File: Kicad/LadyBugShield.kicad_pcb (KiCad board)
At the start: 2 copper layers, 81.3 x 53.3 mm, 48 parts, among them P1 CONN_6, P2 CONN_2, P3 BNC, P4 BNC, Q1 TIP122, Q2 TIP122, Q3 TIP122, U1 MCP6244, U2 MCP6242, U3 MC78L05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

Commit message: 2nd iteration on layout
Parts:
- R2: value 1.5K 1% -> 1K 1%
- moved C1 33.1 mm to (222.9, 106.4), turned to 0 degrees
- moved D8 28.8 mm to (210.4, 80.3), turned to 90 degrees
- moved R1 24.7 mm to (184.3, 70.6)
- moved D7 23.2 mm to (194.1, 99.1), turned to 180 degrees
- moved C8 21.3 mm to (219.8, 97.3), turned to 0 degrees
- moved C6 20.9 mm to (202.8, 79.4), turned to 90 degrees
- moved R16 20.8 mm to (215.5, 89.2), turned to 0 degrees
- moved D6 19.2 mm to (193.8, 92.6), turned to 0 degrees
- moved D4 18.1 mm to (206.0, 80.4), turned to 270 degrees
- moved R4 17.7 mm to (209.4, 87.4), turned to 180 degrees
- moved R14 17.5 mm to (215.5, 91.4), turned to 180 degrees
- moved R13 17.4 mm to (208.4, 85.1), turned to 0 degrees
- moved C5 17.2 mm to (211.4, 89.6), turned to 0 degrees
- moved C7 16.0 mm to (215.5, 93.7), turned to 0 degrees
- moved R19 16.0 mm to (215.5, 96.0), turned to 0 degrees
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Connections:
- ARD1 pad 8: /Arduino/ALERT -> (no net)
- U4 pad 2: /Arduino/ALERT -> (no net)
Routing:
- net VClean: track 201.1 -> 264.5 mm, vias 3 -> 4
- net /EC/f1: track 56.5 -> 9.40 mm
- net /DigitalAccess/pH_AIN: track 50.9 -> 71.6 mm, vias 2 -> 0
- net /EC/EC_ProbeIN: track 24.3 -> 44.5 mm, vias 0 -> 2
- net /Arduino/Pump1: track 36.4 -> 20.4 mm
- net N-0000051: track 4.68 -> 18.8 mm
- net /Arduino/ALERT: track 13.8 -> 0.00 mm
- net /DigitalAccess/EC_AIN: track 26.2 -> 15.5 mm, vias 2 -> 0
- net /Pumps/SW_Pump1: track 17.5 -> 24.9 mm
- net VGND: track 136.6 -> 143.4 mm, vias 4 -> 1
- net AC_Shrunk: track 8.64 -> 14.5 mm
- net EC_Signal: track 20.8 -> 14.9 mm
- net /EC/RVin-: track 14.1 -> 19.9 mm
- net N-0000052: track 4.15 -> 8.63 mm
- net /Pumps/SW_Pump2: track 19.3 -> 23.7 mm
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
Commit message: update to 2nd pass of layout
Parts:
- moved R7 1.65 mm to (220.0, 108.9)
- moved R6 1.35 mm to (216.5, 109.0)
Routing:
- net GND: track 53.5 -> 50.0 mm, vias 16 -> 15
- net VClean: track 264.5 -> 262.4 mm
- net /Arduino/SDA: track 9.95 -> 10.8 mm

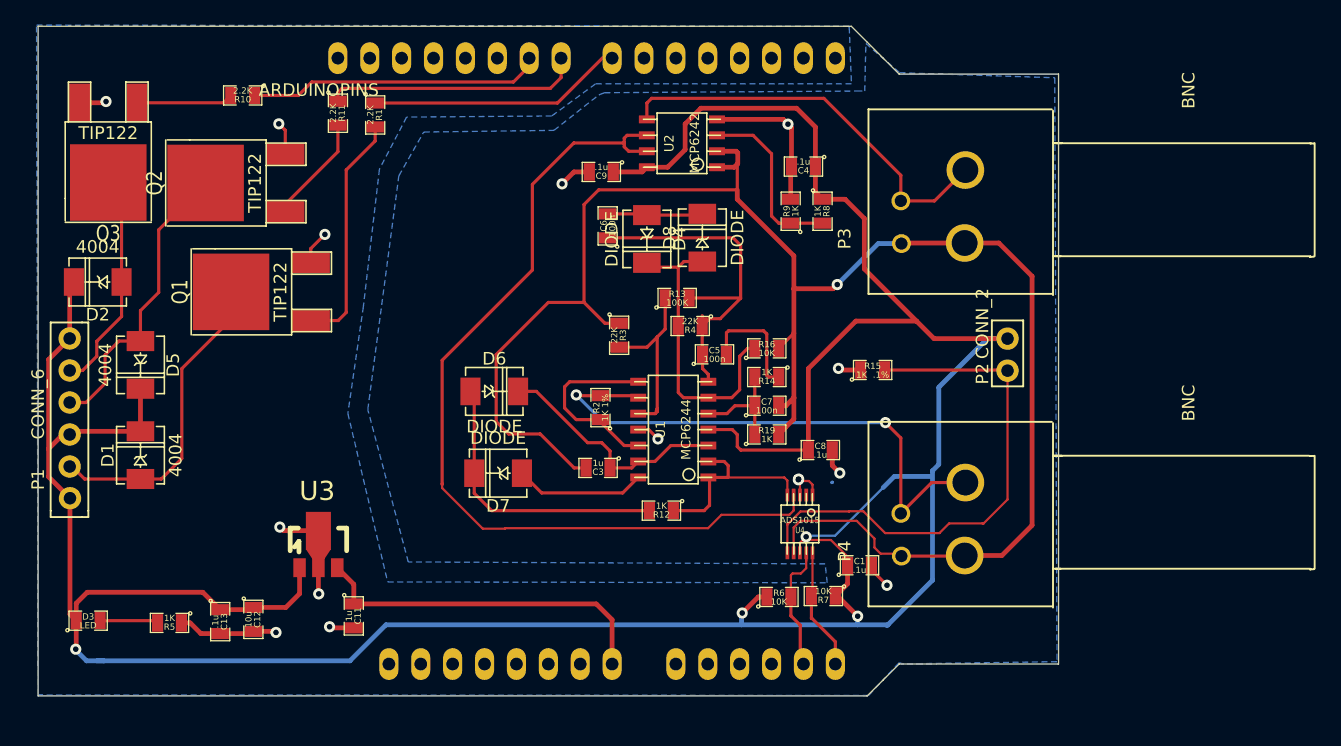
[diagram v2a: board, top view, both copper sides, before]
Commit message: changed diodes added test points
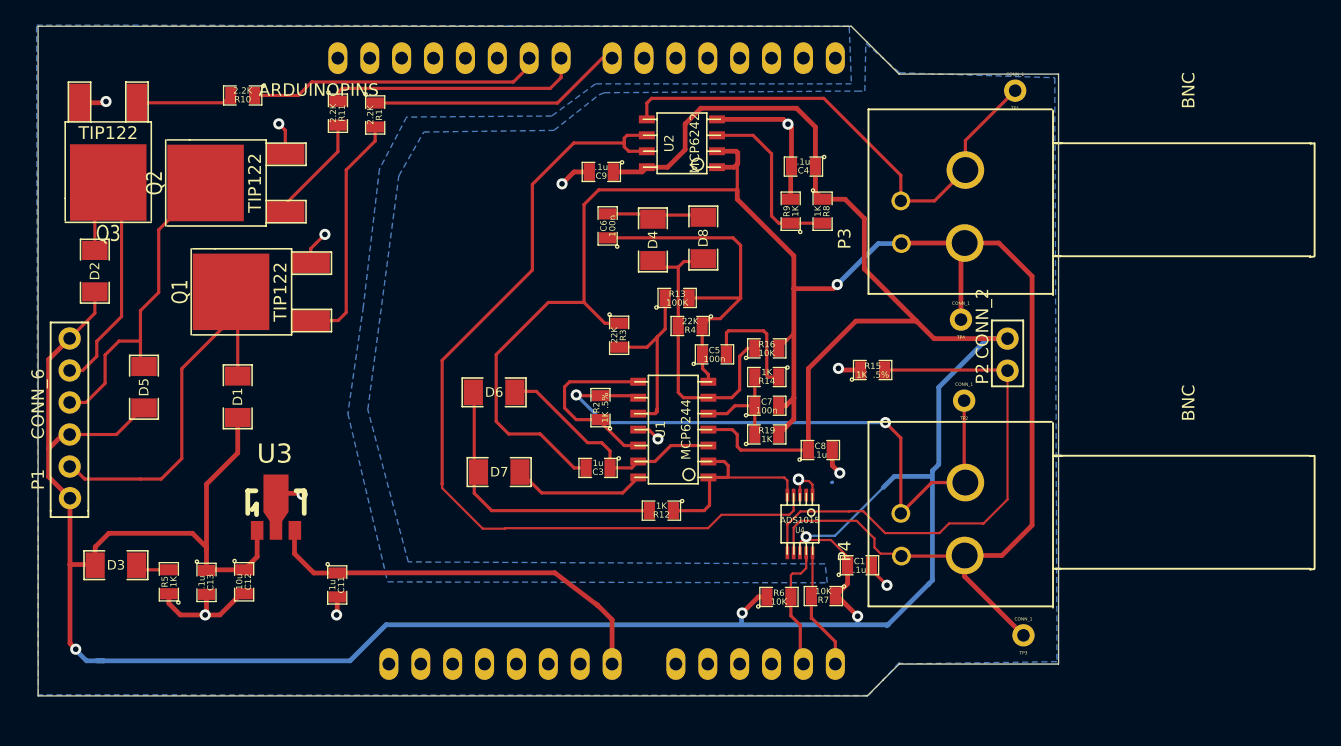
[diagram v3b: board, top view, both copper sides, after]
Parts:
- added TP1: CONN_1, LB_CONN_1, F.Cu at (235.3, 68.6)
- added TP2: CONN_1, LB_CONN_1, F.Cu at (231.2, 93.3)
- added TP3: CONN_1, LB_CONN_1, F.Cu at (236.0, 112.0)
- added TP4: CONN_1, LB_CONN_1, F.Cu at (231.0, 86.9)
- D1, D2, D4, D5, D6, D7, D8: footprint DO-214AC(SMA) -> SM1206
- D3: footprint SM0805 -> SM1206
- R15: value 1K .1% -> 1K .5%
- R2: value 1K 1% -> 1K .5%
- moved D1 9.03 mm to (173.4, 93.0), turned to 270 degrees
- moved D3 4.94 mm to (163.7, 106.4)
- moved U3 4.50 mm to (176.4, 101.8)
- moved C13 3.31 mm to (170.9, 107.8)
- moved R5 3.28 mm to (167.9, 107.7), turned to 90 degrees
- moved C12 3.09 mm to (173.9, 107.7)
- moved C11 2.80 mm to (181.3, 108.0)
- moved D5 1.80 mm to (165.9, 92.3)
- moved D2 0.89 mm to (162.0, 83.0), turned to 270 degrees
- moved D4 0.49 mm to (206.5, 80.5)
- moved D7 0.13 mm to (194.2, 99.0)
- moved D8 0.08 mm to (210.5, 80.4)
- moved D6 0.08 mm to (193.8, 92.7)
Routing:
- net VGND: track 143.4 -> 157.9 mm
- net VClean: track 262.4 -> 270.8 mm
- net /pH/pH_ProbeIN: track 32.4 -> 40.4 mm
- net /Pumps/SW_Pump1: track 24.9 -> 31.9 mm
- net /EC/EC_ProbeIN: track 44.5 -> 51.0 mm
- net /Pumps/SW_Pump3: track 17.7 -> 23.6 mm
- net Vin: track 28.1 -> 33.0 mm
- net /Pumps/SW_Pump2: track 23.7 -> 26.0 mm
- net N-0000053: track 4.65 -> 2.72 mm
- net GND: track 50.0 -> 50.8 mm, vias 15 -> 14
- net /EC/W_Vout: track 28.6 -> 27.8 mm
- net (no net): track 0.57 -> 0.06 mm

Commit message: moved component reference and value for placing components
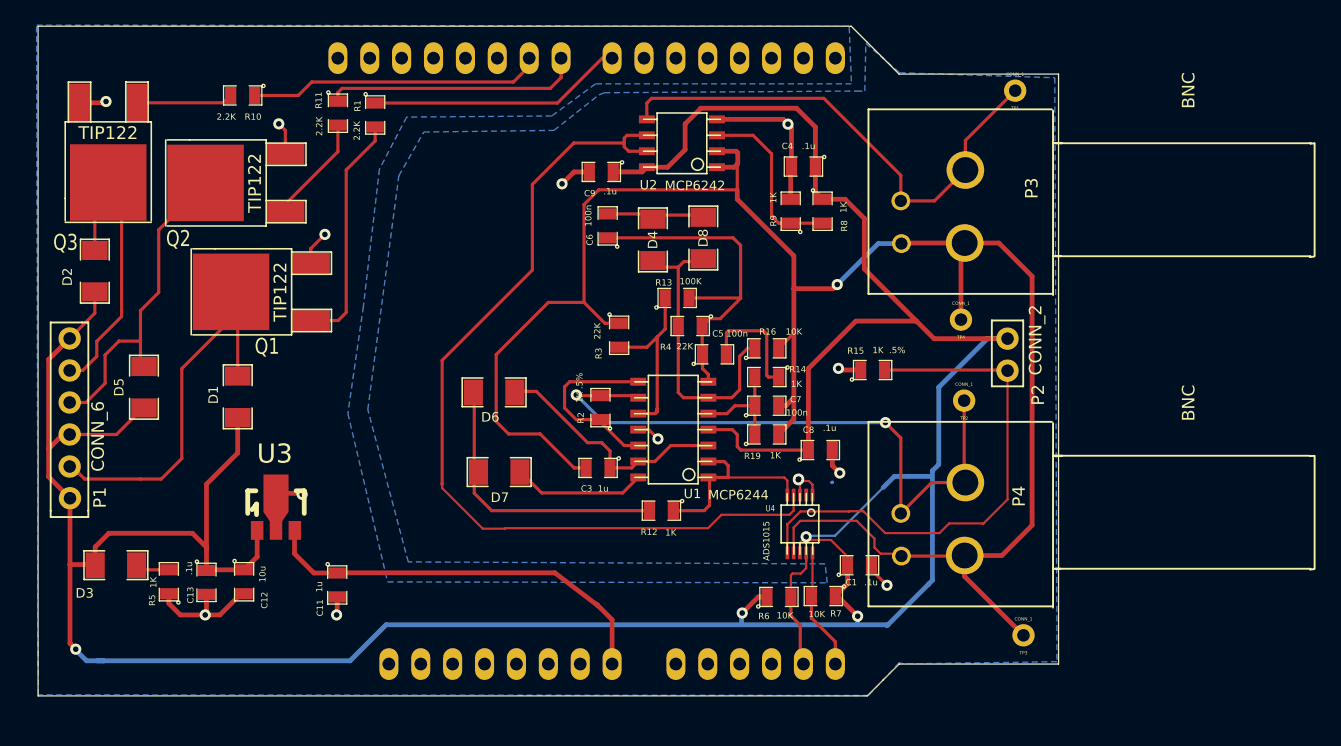
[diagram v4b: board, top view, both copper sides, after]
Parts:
- ARD1: value ARDUINOPINS -> ~
- D1: value 4004 -> ~
- D5: value 4004 -> (none)
- D6: value DIODE -> (none)
- D7: value DIODE -> ~

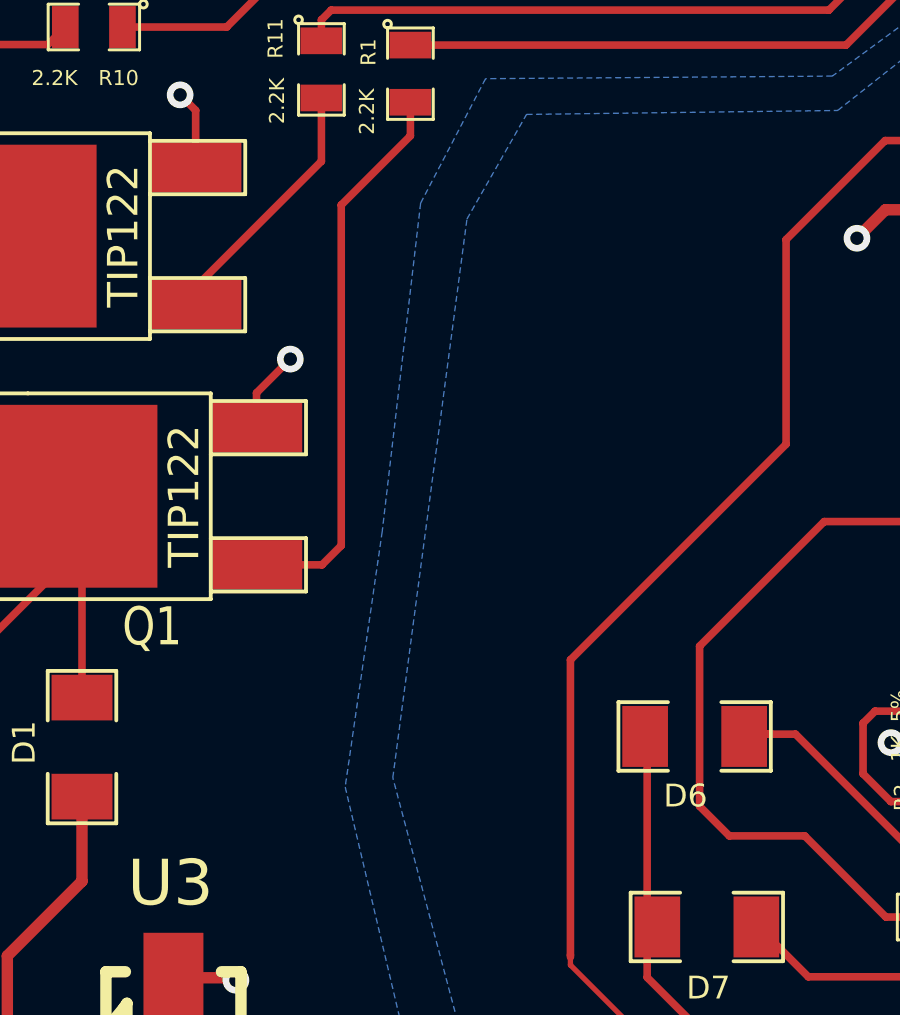
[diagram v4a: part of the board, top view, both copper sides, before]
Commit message: added graphics to layout
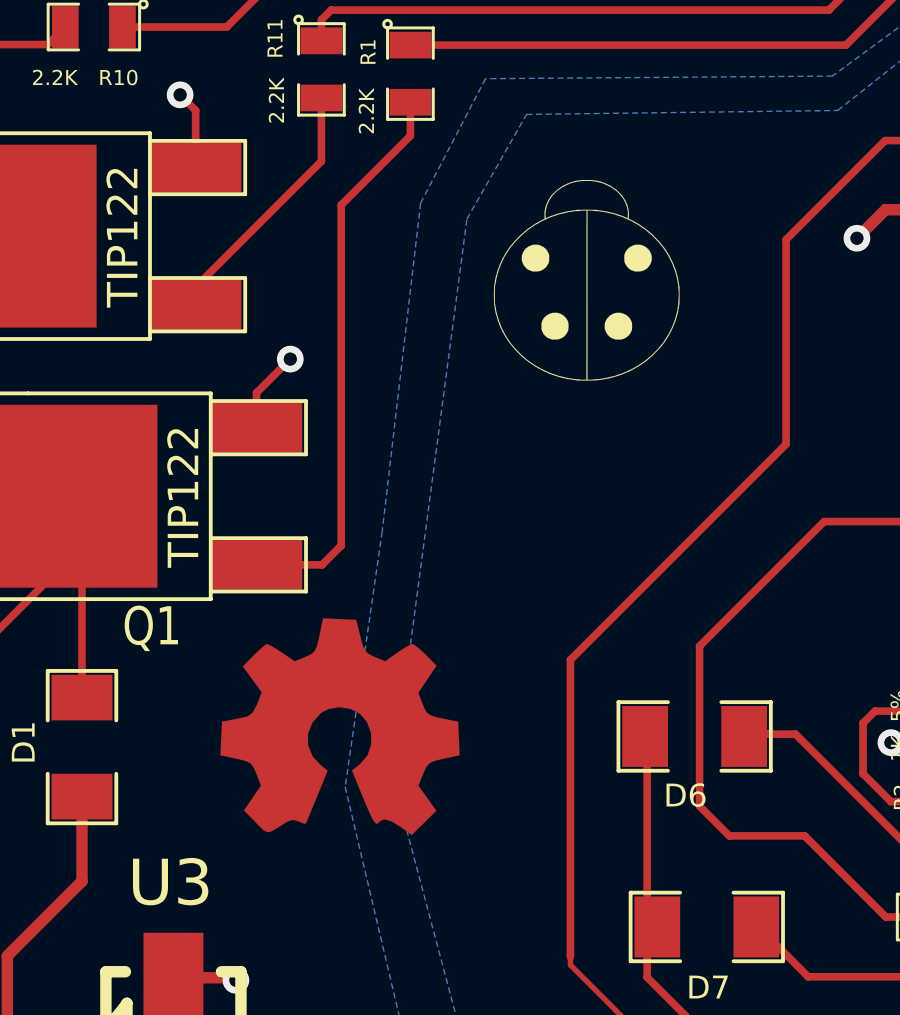
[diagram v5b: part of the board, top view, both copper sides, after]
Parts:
- added ?: , Ladybug_small, F.Cu at (190.2, 77.5)
- added ~: ~, OSHW_CU, B.SilkS at (182.1, 92.5)
- added ~: ~, OSHW_SM, B.SilkS at (182.1, 92.5)

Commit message: changes to layout after 12/22/2014 helpout
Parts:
- ARD1: value ~ -> ARDUINOPINS
- D1: value ~ -> 4004
- D5: value (none) -> 4004
- D6: value (none) -> DIODE
- D7: value ~ -> DIODE
- moved D7 26.1 mm to (216.8, 85.8), turned to 0 degrees
- moved D6 23.4 mm to (217.0, 89.3), turned to 180 degrees
- moved R3 18.3 mm to (220.9, 94.5)
- moved R14 17.0 mm to (199.7, 97.8), turned to 0 degrees
- moved C3 16.0 mm to (216.6, 92.0), turned to 0 degrees
- moved R19 15.9 mm to (199.7, 95.5), turned to 180 degrees
- moved C7 15.8 mm to (199.7, 93.0), turned to 180 degrees
- moved R16 15.8 mm to (199.8, 90.2), turned to 180 degrees
- moved R2 13.8 mm to (215.5, 97.8)
- moved C1 13.2 mm to (210.0, 109.2), turned to 180 degrees
- moved C5 12.5 mm to (204.3, 79.3), turned to 90 degrees
- moved D8 12.3 mm to (198.5, 83.5), turned to 180 degrees
- moved D4 9.97 mm to (198.7, 86.8), turned to 0 degrees
- moved U4 5.30 mm to (212.9, 103.8)
- moved TP3 4.89 mm to (231.3, 110.4)
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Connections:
- U1 pad 1: /DigitalAccess/EC_AIN -> EC_Signal
- U1 pad 10: AC_Shrunk -> /EC/W_Vin+
- U1 pad 12: EC_Signal -> /EC/RVin-
- U1 pad 13: /EC/RVin- -> /DigitalAccess/EC_AIN
- U1 pad 14: /EC/R_Vout -> /DigitalAccess/EC_AIN
- U1 pad 2: /DigitalAccess/EC_AIN -> /EC/EC_ProbeIN
- U1 pad 3: /EC/RVin- -> AC_Shrunk
- U1 pad 5: /EC/W_Vin+ -> EC_Signal
- U1 pad 6: /EC/W_Vin- -> /EC/RVin-
- U1 pad 7: /EC/W_Vout -> /EC/R_Vout
- U1 pad 8: EC_Signal -> /EC/W_Vout
- U1 pad 9: /EC/EC_ProbeIN -> /EC/W_Vin-
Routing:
- net /EC/f1: track 9.40 -> 34.4 mm
- net /EC/EC_ProbeIN: track 51.0 -> 28.6 mm, vias 2 -> 0
- net VClean: track 270.8 -> 290.3 mm, vias 4 -> 1
- net /EC/W_Vout: track 27.8 -> 15.2 mm
- net /EC/DD: track 22.8 -> 35.3 mm, vias 0 -> 3
- net VGND: track 157.9 -> 146.5 mm, vias 1 -> 0
- net /EC/RVin-: track 19.9 -> 12.9 mm
- net /EC/W_Vin-: track 24.2 -> 17.6 mm
- net /Arduino/SCL: track 9.72 -> 15.7 mm
- net /EC/G1: track 7.62 -> 13.5 mm
- net /DigitalAccess/pH_AIN: track 71.6 -> 66.8 mm
- net /EC/R_Vout: track 10.4 -> 6.30 mm
- net EC_Signal: track 14.9 -> 11.2 mm
- net /DigitalAccess/EC_AIN: track 15.5 -> 12.0 mm
- net AC_Shrunk: track 14.5 -> 17.7 mm, vias 0 -> 2
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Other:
- board size 81.3 x 53.3 mm -> 81.3 x 55.3 mm
- net class VClean added: clearance 0.254, trace_width 0.6096, via_dia 0.889, via_drill 0.635
